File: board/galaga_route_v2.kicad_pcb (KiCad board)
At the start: 2 copper layers, 78.7 x 53.3 mm, 18 parts, among them J1 led_a, J2 speaker_out, J3 led_b, J4 led_c, J5 pwr_in, Q1 2N7000, SW1 SW_Push, U1 LD1117S33TR_SOT223, U2 ATmega328P-PU, U3 LM386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

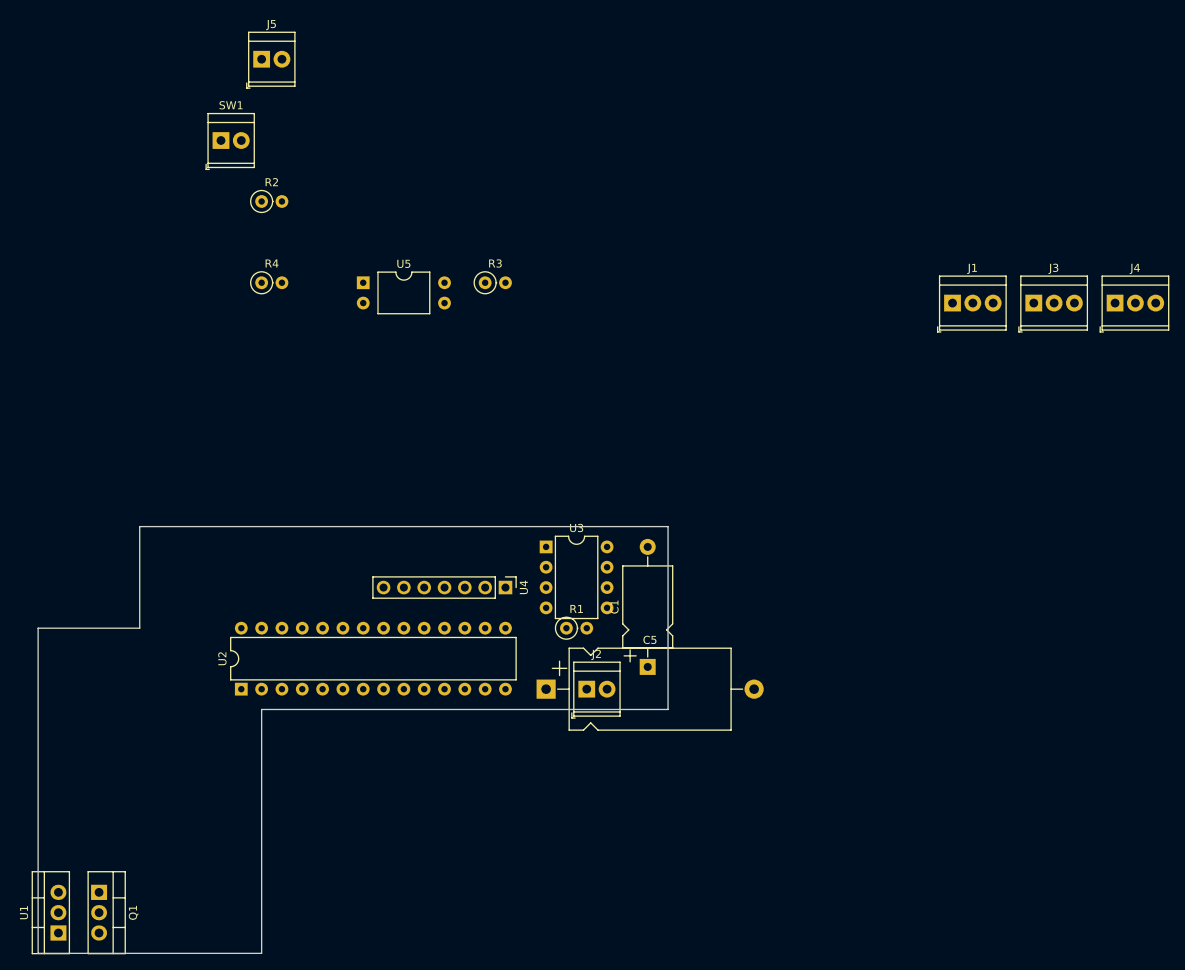
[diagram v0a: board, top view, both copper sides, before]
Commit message: changed SD CS pin to PORTB7 for better board layout
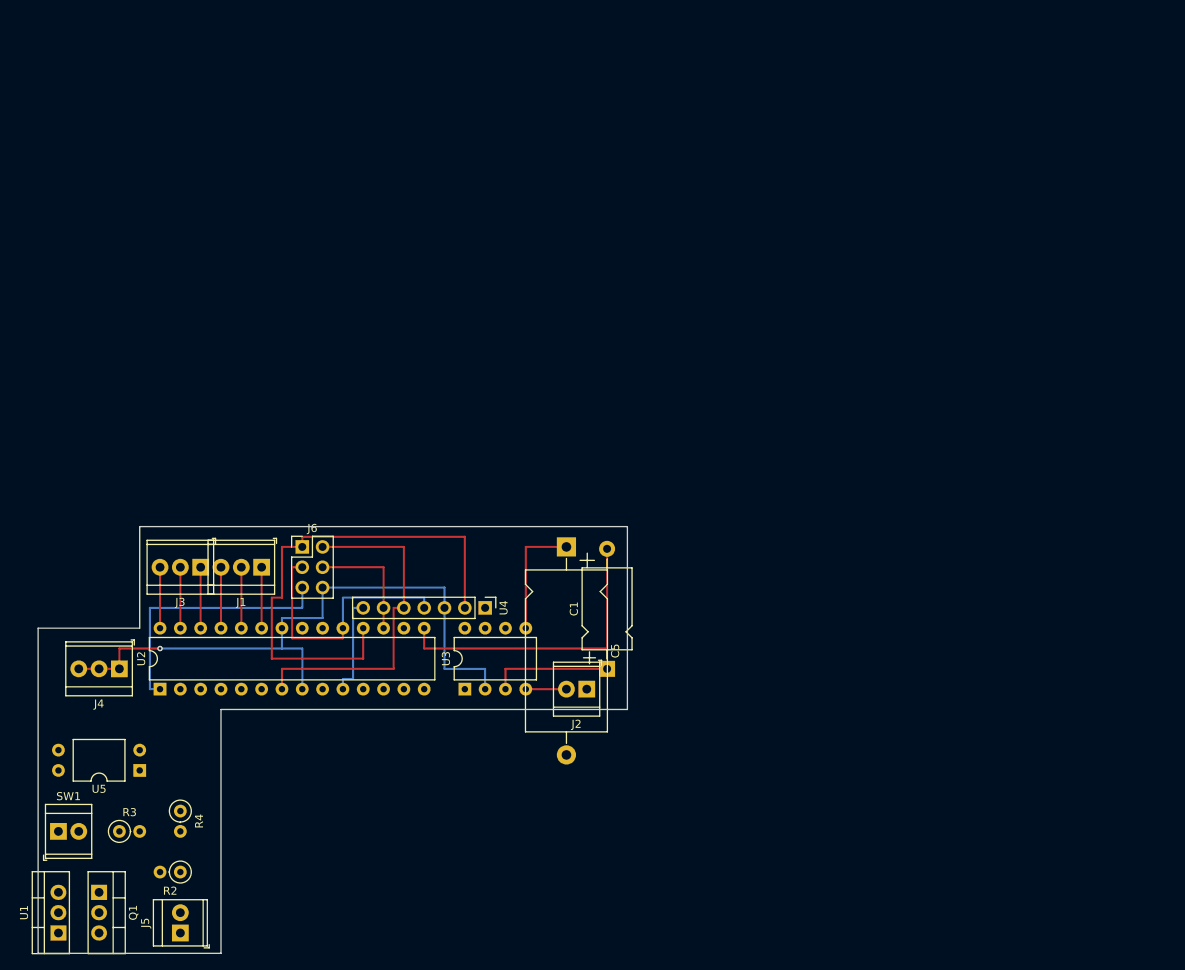
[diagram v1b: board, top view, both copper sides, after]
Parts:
- removed R1: 3.9k, Resistor_THT:R_Axial_DIN0207_L6.3mm_D2.5mm_P2.54mm_Vertical
- added J6: Conn_02x03_Odd_Even, Connector_PinHeader_2.54mm:PinHeader_2x03_P2.54mm_Vertical, F.Cu at (58.4, 127.0)
- moved J4 132.6 mm to (35.6, 142.2), turned to 180 degrees
- moved J5 109.7 mm to (43.2, 175.3), turned to 90 degrees
- moved J3 109.2 mm to (45.7, 129.5), turned to 180 degrees
- moved J1 92.5 mm to (53.3, 129.5), turned to 180 degrees
- moved SW1 88.7 mm to (27.9, 162.6)
- moved R2 84.4 mm to (43.2, 167.6), turned to 180 degrees
- moved R3 82.4 mm to (35.6, 162.6)
- moved U5 67.1 mm to (38.1, 154.9), turned to 180 degrees
- moved R4 66.8 mm to (43.2, 160.0), turned to 270 degrees
- moved U3 20.5 mm to (78.7, 144.8), turned to 90 degrees
- moved C5 18.0 mm to (91.4, 127.0), turned to 270 degrees
- moved U2 10.2 mm to (40.6, 144.8)
- moved C1 5.09 mm to (96.5, 142.2)
- moved U4 3.59 mm to (81.3, 134.6)
- turned J2 to 180 degrees
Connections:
- U2 pad 10: Net-(U2-Pad10) -> /sd_cs
- U2 pad 15: Net-(R1-Pad1) -> Net-(C1-Pad2)
- U2 pad 16: /sd_cs -> Net-(U2-Pad16)
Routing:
- net DGND: track 0.00 -> 81.3 mm, vias 0 -> 1
- net /sd_do: track 0.00 -> 63.5 mm
- net +3V3: track 0.00 -> 43.2 mm
- net Net-(C1-Pad2): track 0.00 -> 38.1 mm
- net /sd_sck: track 0.00 -> 33.0 mm
- net Net-(J6-Pad5): track 0.00 -> 33.0 mm
- net /sd_di: track 0.00 -> 15.2 mm
- net Net-(C5-Pad1): track 0.00 -> 15.2 mm
- net Net-(C1-Pad1): track 0.00 -> 15.2 mm
- net /sd_cs: track 0.00 -> 12.7 mm
- net /led_bs1: track 0.00 -> 7.62 mm
- net /led_bs0: track 0.00 -> 7.62 mm
- net /led_bl3: track 0.00 -> 7.62 mm
- net /led_bl2: track 0.00 -> 7.62 mm
- net /led_bl1: track 0.00 -> 7.62 mm
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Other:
- board size 78.7 x 53.3 mm -> 73.7 x 53.3 mm

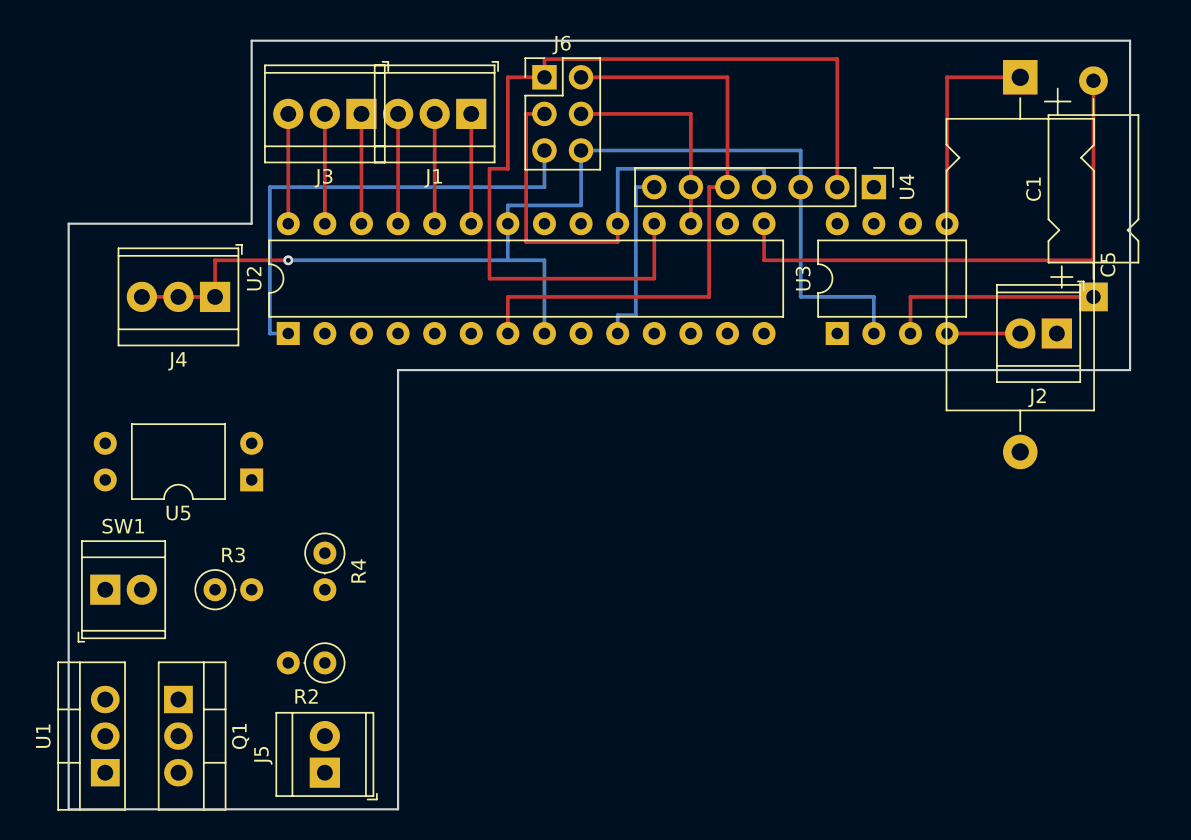
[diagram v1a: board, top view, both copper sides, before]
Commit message: revamped power and amp circuits, going back to breadboard testing before circuit construction
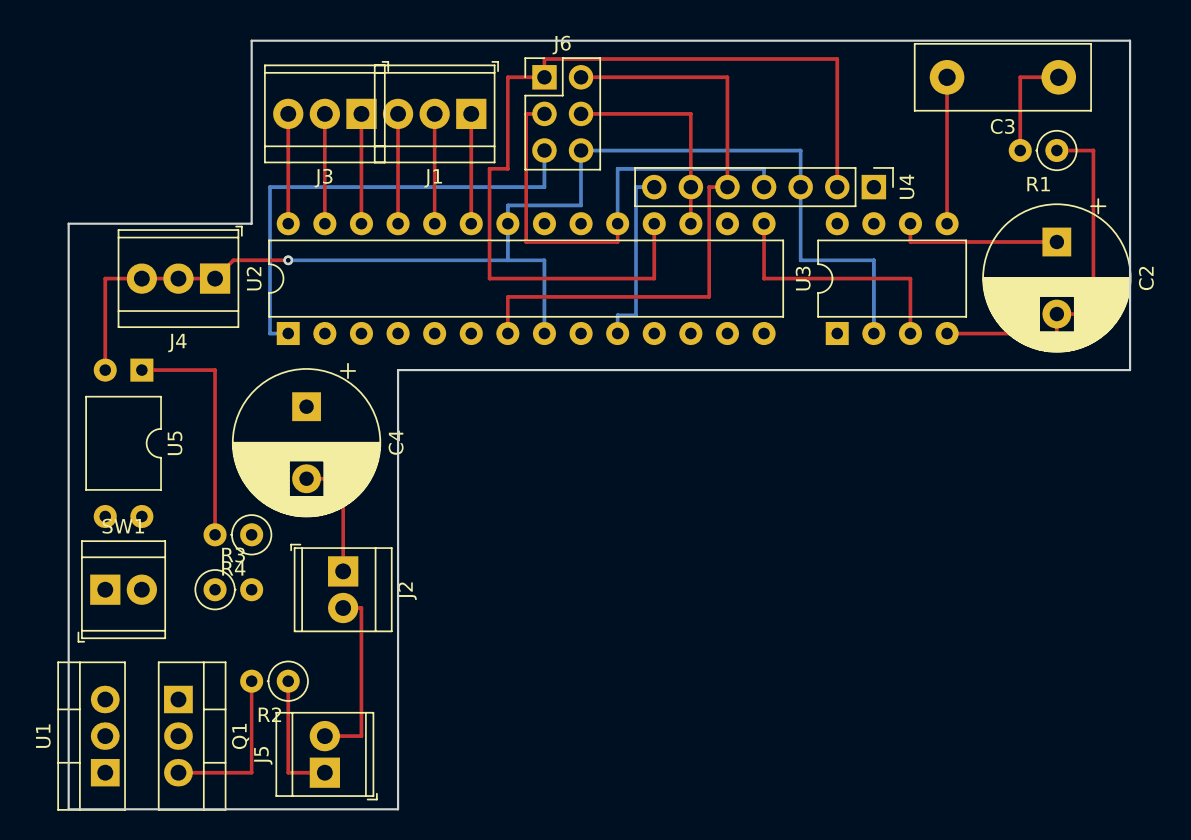
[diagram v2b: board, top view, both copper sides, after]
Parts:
- removed C1: 10uF, Capacitor_THT:CP_Axial_L10.0mm_D6.0mm_P15.00mm_Horizontal
- removed C5: 250uF, Capacitor_THT:CP_Axial_L20.0mm_D10.0mm_P26.00mm_Horizontal
- added C2: 330uF, Capacitor_THT:CP_Radial_D10.0mm_P5.00mm, F.Cu at (94.0, 138.4)
- added C3: 0.05uF, Capacitor_THT:C_Disc_D12.0mm_W4.4mm_P7.75mm, F.Cu at (94.1, 127.0)
- added C4: 330uF, Capacitor_THT:CP_Radial_D10.0mm_P5.00mm, F.Cu at (41.9, 149.9)
- added R1: 10R, Resistor_THT:R_Axial_DIN0207_L6.3mm_D2.5mm_P2.54mm_Vertical, F.Cu at (94.0, 132.1)
- moved J2 52.2 mm to (44.5, 161.3), turned to 270 degrees
- moved U5 10.8 mm to (30.5, 147.3), turned to 270 degrees
- moved R4 5.24 mm to (38.1, 158.8), turned to 180 degrees
- moved R2 2.84 mm to (40.6, 168.9)
- moved J4 1.27 mm to (35.6, 141.0)
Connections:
- U2 pad 15: Net-(C1-Pad2) -> Net-(U2-Pad15)
- U3 pad 3: Net-(C1-Pad1) -> Net-(U2-Pad15)
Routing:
- net Net-(C1-Pad2): track 38.1 -> 0.00 mm
- net BGND: track 5.08 -> 38.2 mm
- net +9V: track 0.00 -> 20.3 mm
- net DGND: track 81.3 -> 99.6 mm
- net Net-(U2-Pad15): track 0.00 -> 17.8 mm
- net Net-(R4-Pad2): track 0.00 -> 16.5 mm
- net Net-(C1-Pad1): track 15.2 -> 0.00 mm
- net Net-(C4-Pad2): track 0.00 -> 8.92 mm
- net Net-(C3-Pad1): track 0.00 -> 7.75 mm
- net Net-(C3-Pad2): track 15.2 -> 10.2 mm

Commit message: finished the board, worked first shot!
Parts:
- Q1: value 2N7000 -> IRF540N
- R2: value 10M -> 10k
- R3: value 20K -> 10K
- moved R4 11.7 mm to (35.6, 147.3)
- moved U1 7.18 mm to (33.0, 170.2), turned to 270 degrees
- moved Q1 6.35 mm to (26.7, 170.2)
- moved R3 2.84 mm to (36.8, 160.0), turned to 180 degrees
- moved R2 2.54 mm to (43.2, 168.9)
- moved SW1 2.54 mm to (30.5, 162.6), turned to 180 degrees
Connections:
- C2 pad 2: BGND -> DGND
- J2 pad 2: BGND -> DGND
- J5 pad 2: BGND -> GND
- Q1 pad 1: BGND -> Net-(Q1-Pad1)
- Q1 pad 2: Net-(Q1-Pad2) -> DGND
- Q1 pad 3: DGND -> GND
- R1 pad 1: BGND -> DGND
- R3 pad 1: Net-(R3-Pad1) -> GND
- R3 pad 2: Net-(Q1-Pad2) -> Net-(Q1-Pad1)
- SW1 pad 2: Net-(R3-Pad1) -> Net-(Q1-Pad1)
- U3 pad 4: BGND -> DGND
- U5 pad 3: BGND -> Net-(Q1-Pad1)
- U5 pad 4: Net-(Q1-Pad2) -> +9V
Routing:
- net +9V: track 20.3 -> 119.5 mm, vias 0 -> 1
- net DGND: track 99.6 -> 182.2 mm
- net Net-(C3-Pad2): track 10.2 -> 70.7 mm
- net +3V3: track 43.2 -> 97.7 mm, vias 0 -> 1
- net BGND: track 38.2 -> 0.00 mm
- net GND: track 0.00 -> 35.6 mm
- net PWR_OFF: track 0.00 -> 27.2 mm
- net Net-(Q1-Pad1): track 0.00 -> 24.7 mm
- net Net-(R4-Pad2): track 16.5 -> 2.54 mm

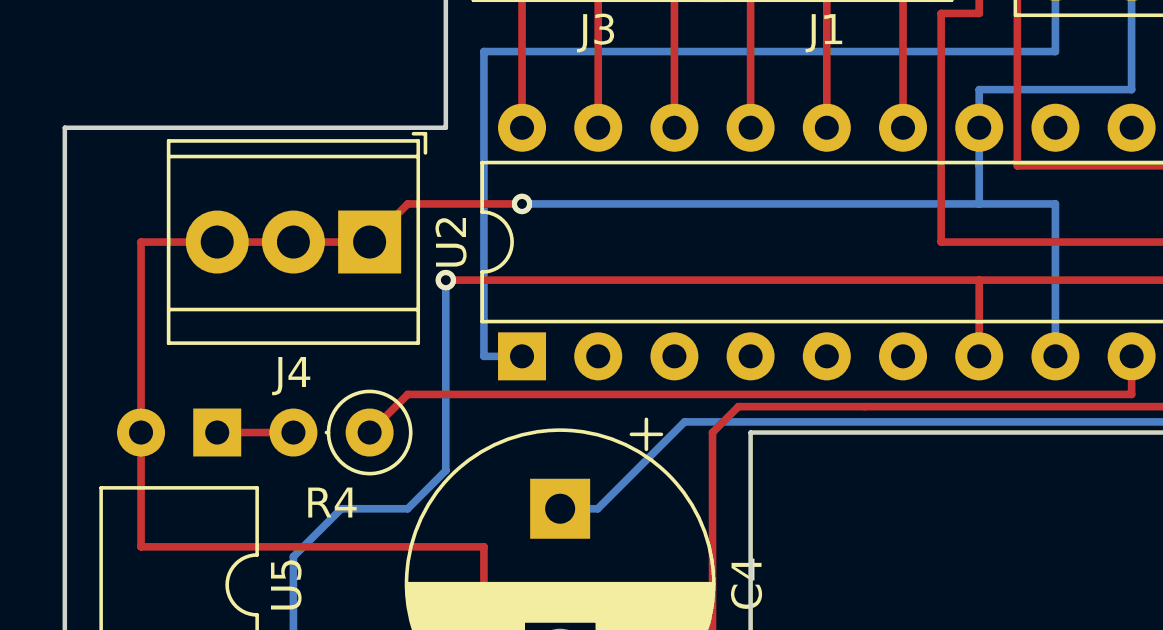
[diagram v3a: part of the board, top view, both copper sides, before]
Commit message: led flashing demo implemented, broke rng...
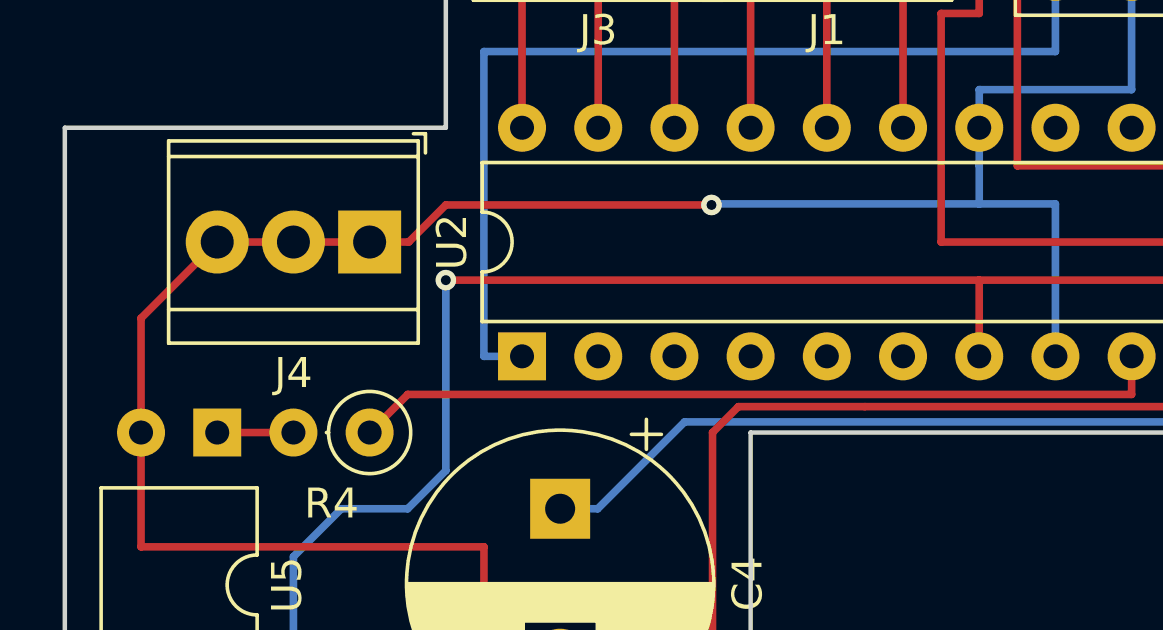
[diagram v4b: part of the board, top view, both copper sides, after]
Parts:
- R3: value 10K -> 10k
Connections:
- R3 pad 1: GND -> Net-(R3-Pad1)
- R3 pad 2: Net-(Q1-Pad1) -> GND
- U2 pad 20: Net-(U2-Pad20) -> +3V3
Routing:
- net DGND: track 182.2 -> 180.7 mm
